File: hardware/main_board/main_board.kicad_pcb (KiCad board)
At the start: 2 copper layers, 12 parts, among them J1 Conn_01x01_Pin, J2 Conn_01x02_Pin, J3 Conn_02x12_Odd_Even, J4 Conn_02x12_Odd_Even, J5 SJ3-35083C-TR, J6 SJ3-35083C-TR, J7 Barrel_Jack_Switch_Pin3Ring, U1 CD40109BE, U2 L78M05CV

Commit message: Improve robustness of prototype with daisy seed
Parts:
- moved A1 19.9 mm to (117.9, 64.0)
- moved A2 19.7 mm to (80.5, 51.1)
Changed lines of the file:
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@@
 	(footprint "Module:Arduino_Nano"
 		(layer "F.Cu")
-		(at 129.032 47.498)
+		(at 117.856 64.008)
 		(descr "Arduino Nano, http://www.mouser.com/pdfdocs/Gravitech_Arduino_Nano3_0.pdf")
 		(tags "Arduino Nano")
@@
 	(footprint "Module:Electrosmith_Daisy_Seed"
 		(layer "F.Cu")
-		(at 96.52 62.484)
+		(at 80.518 51.054)
 		(descr "Embedded platform for audio applications. 96kHz / 24-bit audio hardware. 64MB of SDRAM for up to 10 minute long audio. ARM Cortex-M7 MCU, running at 480MHz. 31 total GPIO pins with configurable functionality. 12-bit Digital to Analog Converters (x2). SD card interfaces. PWM outputs. Serial Protocols for connecting external sensors and devices (SPI, UART, I2S, I2C). Dedicated VIN pin for power. Micro USB port, and additional USB pins for full OTG-support as host and device. https://static1.squarespace.com/static/58d03fdc1b10e3bf442567b8/t/6227e6236f02fb68d1577146/1646781988478/Daisy_Seed_datasheet_v1.0.3.pdf")
 		(tags "Electrosmith Daisy Seed Microcontroller Module ARM Cortex-M7 Audio Codec")
 		(property "Reference" "A2"
-			(at 7.62 -3.6 0)
+			(at 7.62 -3.6 360)
 			(layer "F.SilkS")
 			(effects
@@
 		)
 		(property "Value" "Electrosmith_Daisy_Seed_Rev4"
-			(at 7.62 51 0)
+			(at 7.62 51 360)
 			(layer "F.Fab")
 			(effects
@@
 		)
 		(fp_text user "${REFERENCE}"
-			(at 7.62 22 0)
-			(layer "F.Fab")
-			(effects
+			(at 7.62 22 360)
+			(layer "F.Fab")
+			(effects

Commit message: First test passed with main boards and all satellite boards connected
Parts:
- removed C1: B32529C0102K289, B32529C0102K289:CAPRR500W50L730T250H650
- removed the J6 at (159.8, 94.2)
- removed the U1 at (189.2, 81.8)
- added J4: SD CARD Reader, DM3D_SF:HRS_DM3D-SF, F.Cu at (165.7, 119.0)
- added J7: SJ3-35083C-TR, SJ3_35083C_TR:SAMESKY_SJ3-35083C-TR, F.Cu at (171.5, 85.3)
- added R1: 2.4 KOhm, CF14JT4K70:STA_CF14_STP, F.Cu at (124.1, 105.7)
- added R2: 4.7 KOhm, CF14JT4K70:STA_CF14_STP, F.Cu at (109.1, 105.7)
- added R3: 47 KOhms, 4606X_101_473LF:BO_4606X, F.Cu at (156.2, 111.0)
- added R4: 4.7 KOhm, CF14JT4K70:STA_CF14_STP, F.Cu at (149.0, 94.7)
- A2: value Electrosmith_Daisy_Seed_Rev4 -> Electrosmith_Daisy_Seed
- J5: value SJ3-35083C-TR -> USB typ A; footprint SJ3_35083C_TR:SAMESKY_SJ3-35083C-TR -> 676433910:CONN_67643-3910_MOL
- moved A2 78.7 mm to (95.8, 128.3), turned to 90 degrees
- moved J8 62.7 mm to (165.4, 56.1)
- moved J3 61.2 mm to (171.4, 58.7)
- moved J6 57.8 mm to (166.4, 69.6), turned to 90 degrees
- moved J2 39.6 mm to (123.4, 55.9), turned to -90 degrees
- moved J1 28.8 mm to (158.2, 55.9), turned to -90 degrees
- moved A1 25.1 mm to (106.4, 86.3), turned to 90 degrees
- moved J5 16.7 mm to (165.8, 104.3), turned to 90 degrees
- moved U1 7.50 mm to (152.1, 105.7), turned to 90 degrees
- renumbered J3 to J1, J4 to J2, J1 to J3, J7 to J6, J2 to J8, U2 to U1
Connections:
- A1 pad 1: Net-(A1-TX1) -> Net-(A1-D13)
- A1 pad 10: Net-(A1-D7) -> Net-(A1-A6)
- A1 pad 11: Net-(A1-D8) -> unconnected-(A1-A7-Pad11)
- A1 pad 12: Net-(A1-D9) -> unconnected-(A1-+5V-Pad12)
- A1 pad 13: Net-(A1-D10) -> unconnected-(A1-~{RESET}-Pad13)
- A1 pad 14: Net-(A1-MOSI) -> GND
- A1 pad 15: Net-(A1-MISO) -> Vin
- A1 pad 16: Net-(A1-SCK) -> Net-(A1-TX)
- A1 pad 19: Net-(A1-A0) -> GND
- A1 pad 2: Net-(A1-RX1) -> unconnected-(A1-3V3-Pad2)
- A1 pad 20: Net-(A1-A1) -> Net-(A1-D2)
- A1 pad 21: Net-(A1-A2) -> Net-(A1-D3)
- A1 pad 22: Net-(A1-A3) -> Net-(A1-D4)
- A1 pad 23: Net-(A1-SDA/A4) -> Net-(A1-D5)
- A1 pad 24: Net-(A1-SCL/A5) -> Net-(A1-D6)
- A1 pad 25: Net-(A1-A6) -> Net-(A1-D7)
- A1 pad 26: unconnected-(A1-A7-Pad26) -> Net-(A1-D8)
- A1 pad 27: unconnected-(A1-+5V-Pad27) -> Net-(A1-D9)
- A1 pad 28: unconnected-(A1-~{RESET}-Pad28) -> Net-(A1-D10)
- A1 pad 29: GND -> Net-(A1-D11)
- A1 pad 30: Vin -> Net-(A1-D12)
- A1 pad 4: GND -> Net-(A1-A0)
- A1 pad 5: Net-(A1-D2) -> Net-(A1-A1)
- A1 pad 6: Net-(A1-D3) -> Net-(A1-A2)
- A1 pad 7: Net-(A1-D4) -> Net-(A1-A3)
- A1 pad 8: Net-(A1-D5) -> Net-(A1-A4)
- A1 pad 9: Net-(A1-D6) -> Net-(A1-A5)
- A2 pad 1: unconnected-(A2-USB_ID-Pad1) -> Net-(A2-USB_ID)
- A2 pad 12: unconnected-(A2-I2C1_SCL-Pad12) -> GND
- A2 pad 14: Net-(A2-USART1_TX) -> unconnected-(A2-USART1_TX-Pad14)
- A2 pad 16: Net-(A2-AUDIO_IN_1) -> unconnected-(A2-AUDIO_IN_1-Pad16)
- A2 pad 17: Net-(A2-AUDIO_IN_2) -> unconnected-(A2-AUDIO_IN_2-Pad17)
- A2 pad 2: unconnected-(A2-SD_DATA_3-Pad2) -> Net-(A2-SD_DATA_3)
- A2 pad 3: unconnected-(A2-SD_DATA_2-Pad3) -> Net-(A2-SD_DATA_2)
- A2 pad 36: unconnected-(A2-USB_D_--Pad36) -> Net-(A2-USB_D_-)
- A2 pad 37: unconnected-(A2-USB_D_+-Pad37) -> Net-(A2-USB_D_+)
- A2 pad 4: unconnected-(A2-SD_DATA_1-Pad4) -> Net-(A2-SD_DATA_1)
- A2 pad 5: unconnected-(A2-SD_DATA_0-Pad5) -> Net-(A2-SD_DATA_0)
- A2 pad 6: unconnected-(A2-SD_CMD-Pad6) -> Net-(A2-SD_CMD)
- A2 pad 7: unconnected-(A2-SD_CLK-Pad7) -> Net-(A2-SD_CLK)
- J1 pad 15: Net-(A1-MOSI) -> Net-(A1-D11)
- J1 pad 16: Net-(A1-MISO) -> Net-(A1-D12)
- J1 pad 17: Net-(A1-SCK) -> Net-(A1-D13)
- J1 pad 18: Net-(A1-SCL/A5) -> Net-(A1-A5)
- J1 pad 5: Net-(A1-SDA/A4) -> Net-(A1-A4)
- J2 pad 15: Net-(A1-MOSI) -> Net-(A1-D11)
- J2 pad 16: Net-(A1-MISO) -> Net-(A1-D12)
- J2 pad 17: Net-(A1-SCK) -> Net-(A1-D13)
- J2 pad 18: Net-(A1-SCL/A5) -> Net-(A1-A5)
- J2 pad 5: Net-(A1-SDA/A4) -> Net-(A1-A4)
- J5 pad 1: GND -> Net-(A2-USB_ID)
- J5 pad 2: Net-(A2-AUDIO_OUT_2) -> Net-(A2-USB_D_-)
- J5 pad 4: unconnected-(J5-Pad4) -> GND
- J6 pad 2: unconnected-(J7-Pad2) -> GND

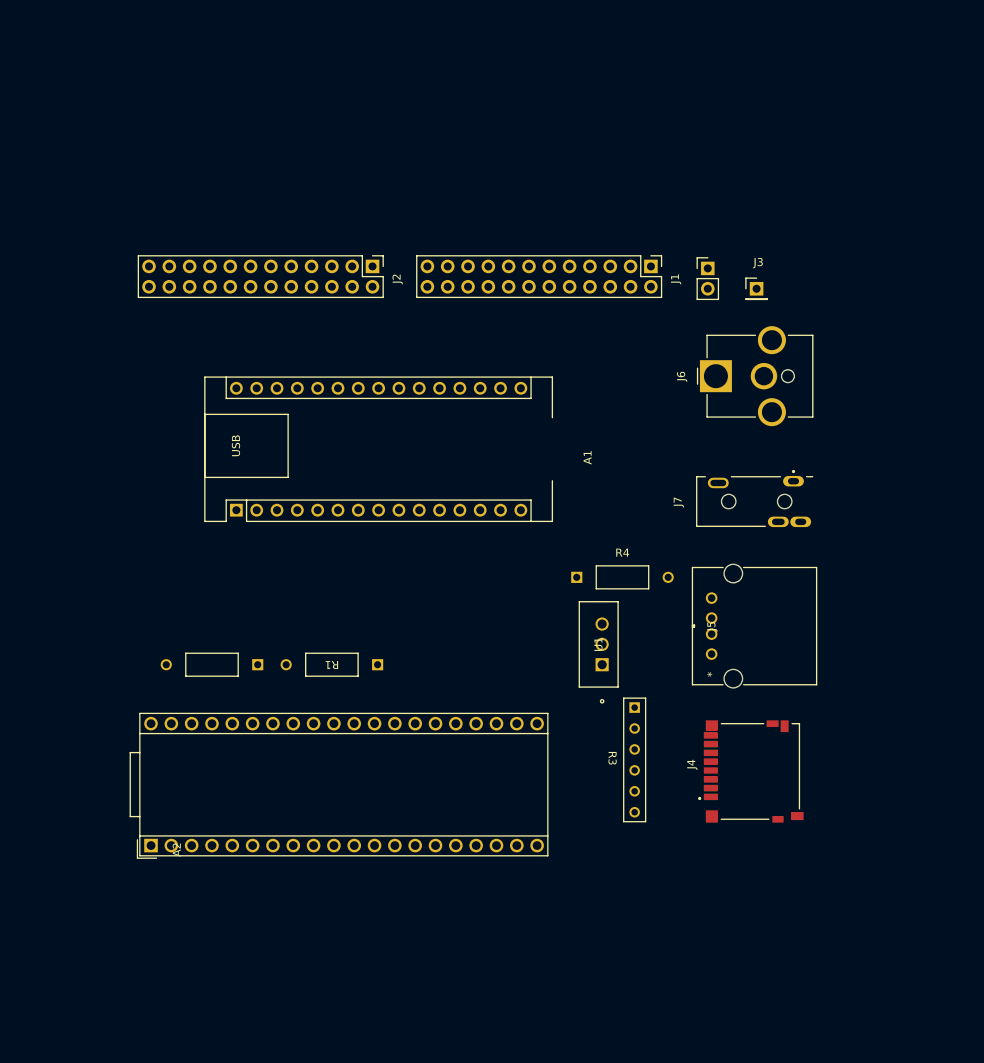
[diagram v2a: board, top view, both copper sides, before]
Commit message: Finish main board PCB
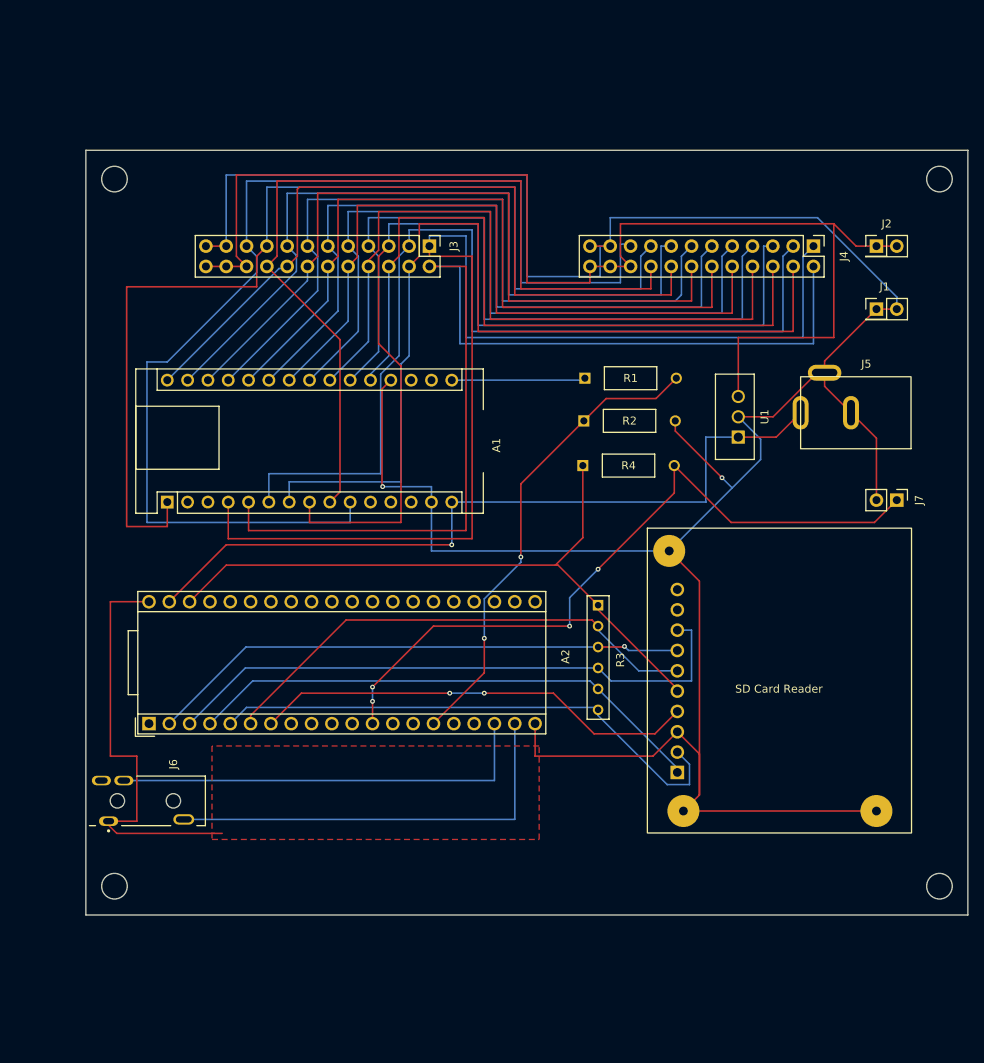
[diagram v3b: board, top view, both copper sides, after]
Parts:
- removed the J3 at (171.4, 58.7)
- removed the J5 at (165.8, 104.3)
- removed J8: Conn_01x02_Pin, Connector_PinHeader_2.54mm:PinHeader_1x02_P2.54mm_Vertical
- added J1: ~, Connector_PinHeader_2.54mm:PinHeader_2x01_P2.54mm_Vertical, F.Cu at (186.4, 61.2)
- added J2: ~, Connector_PinHeader_2.54mm:PinHeader_2x01_P2.54mm_Vertical, F.Cu at (186.4, 53.3)
- added REF**: MountingHole_3.2mm_M3, MountingHole:MountingHole_3.2mm_M3, F.Cu at (91.2, 45.0)
- added REF**: MountingHole_3.2mm_M3, MountingHole:MountingHole_3.2mm_M3, F.Cu at (194.3, 133.3)
- added REF**: MountingHole_3.2mm_M3, MountingHole:MountingHole_3.2mm_M3, F.Cu at (194.3, 45.0)
- added REF**: MountingHole_3.2mm_M3, MountingHole:MountingHole_3.2mm_M3, F.Cu at (91.2, 133.3)
- added SDCardReaderBreakoutBoard1: SD Card Reader, Piano_Library:SD_CARD_READER, F.Cu at (174.2, 107.7)
- J5: renamed from J4; value SD CARD Reader -> Barrel_Jack_Switch_Pin2Ring; footprint DM3D_SF:HRS_DM3D-SF -> Piano_Library:G-1005B
- J6: value Barrel_Jack_Switch_Pin3Ring -> Jack Stereo; footprint Connector_BarrelJack:BarrelJack_CUI_PJ-063AH_Horizontal_CircularHoles -> Piano_Library:SAMESKY_SJ3-35083C-TR
- J7: value SJ3-35083C-TR -> Conn_01x02_Pin; footprint SJ3_35083C_TR:SAMESKY_SJ3-35083C-TR -> Connector_PinHeader_2.54mm:PinHeader_1x02_P2.54mm_Vertical
- R1, R2, R4: footprint CF14JT4K70:STA_CF14_STP -> Piano_Library:STA_CF14_STP
- R3: footprint 4606X_101_473LF:BO_4606X -> Piano_Library:BO_4606X
- U1: footprint L78M05CV:TO-220_STM -> Piano_Library:TO-220_STM
- moved J6 88.9 mm to (95.1, 122.7), turned to -90 degrees
- moved J4 55.2 mm to (178.6, 53.3)
- moved R2 50.9 mm to (149.9, 75.2), turned to 0 degrees
- moved J5 48.3 mm to (183.9, 74.2), turned to 180 degrees
- moved R1 44.2 mm to (150.0, 69.8), turned to 0 degrees
- moved U1 33.1 mm to (169.2, 77.2)
- moved J3 27.8 mm to (130.6, 53.3)
- moved J7 17.5 mm to (189.0, 85.1), turned to -90 degrees
- moved A2 15.2 mm to (95.5, 113.0)
- moved R4 14.0 mm to (149.7, 80.8)
- moved R3 13.6 mm to (151.6, 98.2)
- moved A1 8.70 mm to (97.8, 85.3)
- renumbered J1 to J3, J2 to J4
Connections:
- A2 pad 1: Net-(A2-USB_ID) -> unconnected-(A2-USB_ID-Pad1)
- A2 pad 12: GND -> Net-(A2-I2C1_SCL)
- A2 pad 36: Net-(A2-USB_D_-) -> unconnected-(A2-USB_D_--Pad36)
- A2 pad 37: Net-(A2-USB_D_+) -> unconnected-(A2-USB_D_+-Pad37)
- J5 pad 1: Net-(A2-SD_DATA_2) -> Vin
- J5 pad 2: Net-(A2-SD_DATA_3) -> GND
- J5 pad 3: Net-(A2-SD_CMD) -> GND
- J6 pad 1: Vin -> GND
- J6 pad 2: GND -> Net-(A2-AUDIO_OUT_2)
- J7 pad 1: GND -> Net-(A2-I2C1_SCL)
- J7 pad 2: Net-(A2-AUDIO_OUT_2) -> GND
- R4 pad 2: Net-(J8-Pin_1) -> Net-(A2-I2C1_SCL)
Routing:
- net GND: track 0.00 -> 407.1 mm, vias 0 -> 2
- net VCC: track 0.00 -> 156.4 mm
- net Net-(A1-A0): track 0.00 -> 149.6 mm
- net Net-(A1-A6): track 0.00 -> 144.0 mm
- net Net-(A1-A1): track 0.00 -> 135.6 mm
- net Net-(A1-D13): track 0.00 -> 132.6 mm
- net Net-(A1-A4): track 0.00 -> 123.6 mm
- net Net-(A1-A2): track 0.00 -> 120.1 mm
- net Net-(A1-A3): track 0.00 -> 118.0 mm
- net Net-(A1-A5): track 0.00 -> 108.0 mm
- net Vin: track 0.00 -> 96.6 mm, vias 0 -> 1
- net Net-(A1-D11): track 0.00 -> 96.3 mm
- net Net-(A1-D12): track 0.00 -> 94.9 mm
- net Net-(A1-D9): track 0.00 -> 94.1 mm
- net Net-(A1-D10): track 0.00 -> 93.6 mm
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- added copper zone on F.Cu, net GND
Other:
- board outline added: 110.3 x 95.6 mm
